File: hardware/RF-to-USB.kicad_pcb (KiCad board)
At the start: 4 copper layers, 50 x 20 mm, 52 parts, among them J1 USB_A, J2 SMA-F, J3 ARM SWD, SW1 BTN1, SW2 BTN2, U1 nRF24L01P, U2 STM32L432KBUx, U3 XC6206P332MR, U4 USBLC6-2SC6, U5 OLED Display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

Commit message: routing updates
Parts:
- moved C21 38.3 mm to (98.0, 40.3), turned to 180 degrees
- moved C23 37.3 mm to (99.9, 34.2)
- moved C24 37.3 mm to (102.0, 34.3)
- moved R6 36.6 mm to (98.0, 41.3)
- moved C22 35.5 mm to (98.0, 39.3), turned to 180 degrees
- moved C19 31.7 mm to (92.4, 35.6)
- moved C20 31.7 mm to (92.4, 33.6)
- moved C3 13.7 mm to (100.7, 52.5), turned to 45 degrees
- moved C6 12.6 mm to (93.9, 53.3), turned to 0 degrees
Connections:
- U2 pad 33: GND -> (no net)
- U2 pad 6: BTN1_EXTI -> BTN2_EXTI
- U2 pad 7: BTN2_EXTI -> BTN1_EXTI
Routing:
- net GND: track 76.4 -> 105.2 mm, vias 32 -> 36
- net +3V3: track 22.2 -> 46.7 mm, vias 10 -> 15
- net NRST: track 4.55 -> 29.0 mm, vias 1 -> 2
- net OLED_DC: track 0.00 -> 18.2 mm, vias 0 -> 2
- net SPI3_MOSI: track 8.68 -> 23.3 mm, vias 0 -> 1
- net OLED_CS: track 0.00 -> 14.1 mm, vias 0 -> 2
- net OLED_RES: track 0.00 -> 13.5 mm, vias 0 -> 2
- net Net-(D1-K): track 0.00 -> 8.65 mm, vias 0 -> 1
- net Net-(U5-C2P): track 0.00 -> 6.56 mm
- net Net-(U5-C2N): track 0.00 -> 5.89 mm
- net Net-(U5-C1P): track 0.00 -> 5.23 mm
- net Net-(U5-C1N): track 0.00 -> 4.91 mm
- net +5V: track 11.4 -> 16.1 mm
- net SPI3_SCK: track 12.7 -> 16.1 mm, vias 2 -> 3
- net Net-(U5-VCOMH): track 0.00 -> 3.05 mm, vias 0 -> 1
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
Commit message: routing updates
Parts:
- moved C20 18.7 mm to (87.2, 51.5), turned to 180 degrees
- moved C19 16.2 mm to (89.5, 51.5), turned to 180 degrees
- moved C24 11.0 mm to (101.7, 45.3), turned to 180 degrees
- moved C23 9.27 mm to (97.7, 43.3), turned to 135 degrees
- moved C21 0.25 mm to (98.0, 40.5)
- moved C22 0.25 mm to (98.0, 39.5)
- moved R6 0.25 mm to (98.0, 41.5)
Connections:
- U1 pad 21: (no net) -> GND
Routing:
- net GND: track 105.2 -> 118.3 mm, vias 36 -> 42
- net Net-(U5-C1N): track 4.91 -> 17.2 mm, vias 0 -> 1
- net Net-(U5-C1P): track 5.23 -> 16.1 mm, vias 0 -> 1
- net Net-(U5-C2N): track 5.89 -> 14.7 mm, vias 0 -> 1
- net Net-(U5-C2P): track 6.56 -> 13.6 mm, vias 0 -> 1
- net +5V: track 16.1 -> 22.4 mm, vias 7 -> 6
- net SPI3_SCK: track 16.1 -> 21.2 mm
- net /LED_RX: track 8.27 -> 12.5 mm
- net +3V3: track 46.7 -> 50.8 mm, vias 15 -> 14
- net NRST: track 29.0 -> 31.5 mm
- net Net-(U5-VCC): track 3.00 -> 4.23 mm
- net Net-(U5-IREF): track 2.77 -> 3.92 mm
- net Net-(U5-VCOMH): track 3.05 -> 4.08 mm
- net OLED_DC: track 18.2 -> 19.2 mm, vias 2 -> 1
- net OLED_CS: track 14.1 -> 14.7 mm, vias 2 -> 1
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- added copper zone on B.Cu, net NRST
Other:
- board text added: "R_{x}"
- board text added: "T_{x}"

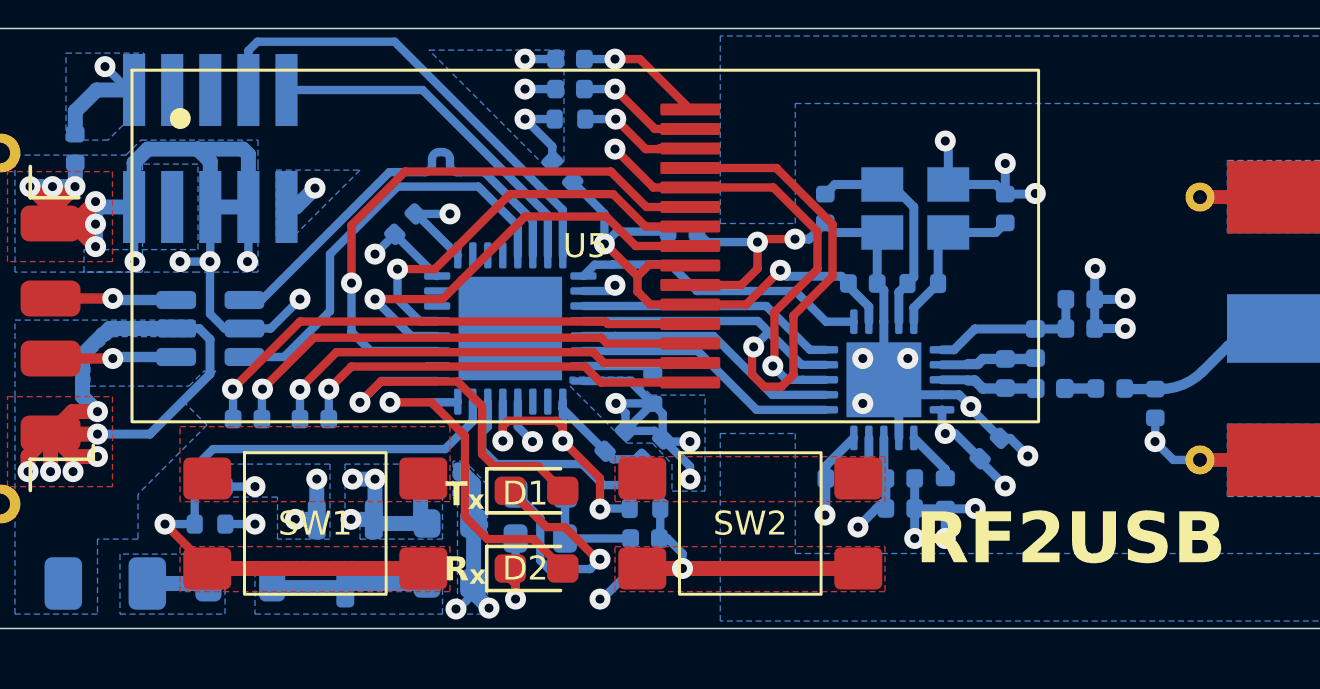
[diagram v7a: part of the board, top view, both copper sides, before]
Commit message: routing updates
all DRC errors & warnings resolved
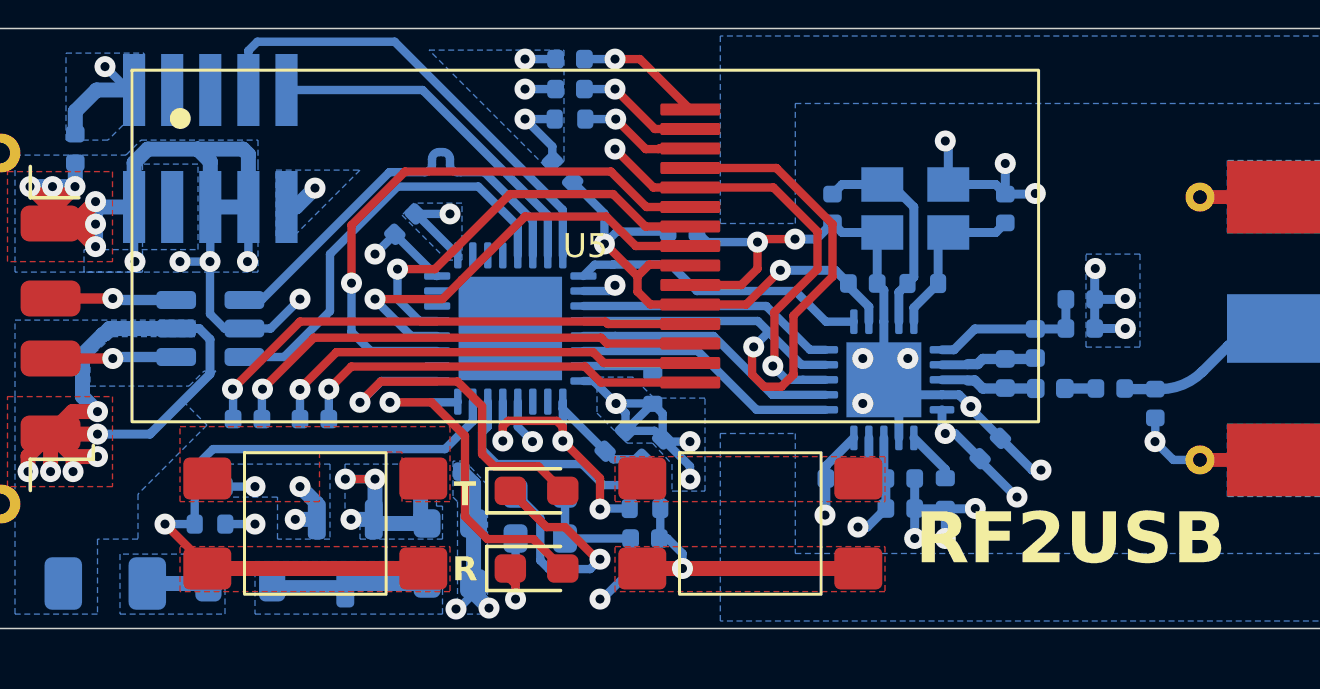
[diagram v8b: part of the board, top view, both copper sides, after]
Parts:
- added G***: LOGO, LOGO, B.Cu at (80.5, 51.6)
- moved C18 0.24 mm to (106.7, 44.5)
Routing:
- net +3V3: track 50.8 -> 52.2 mm
- net GND: track 118.3 -> 117.7 mm
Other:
- board text added: "R"
- board text added: "RemiFM"
- board text added: "T"
- board text removed: "R_{x}"
- board text removed: "T_{x}"
